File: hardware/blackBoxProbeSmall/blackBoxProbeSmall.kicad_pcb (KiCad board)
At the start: 4 copper layers, 44 x 29 mm, 63 parts, among them J1 USB-ID, J2 JTAG_2X05, J3 JTAG_2X05, J4 DevBoardUartOutput, Q1 Q_NMOS_DUAL, Q2 Q_PMOS_DUAL, U1 MCP1702-MB, U2 USBLC6-2, U3 STM32F103CBT, U4 74X2T45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

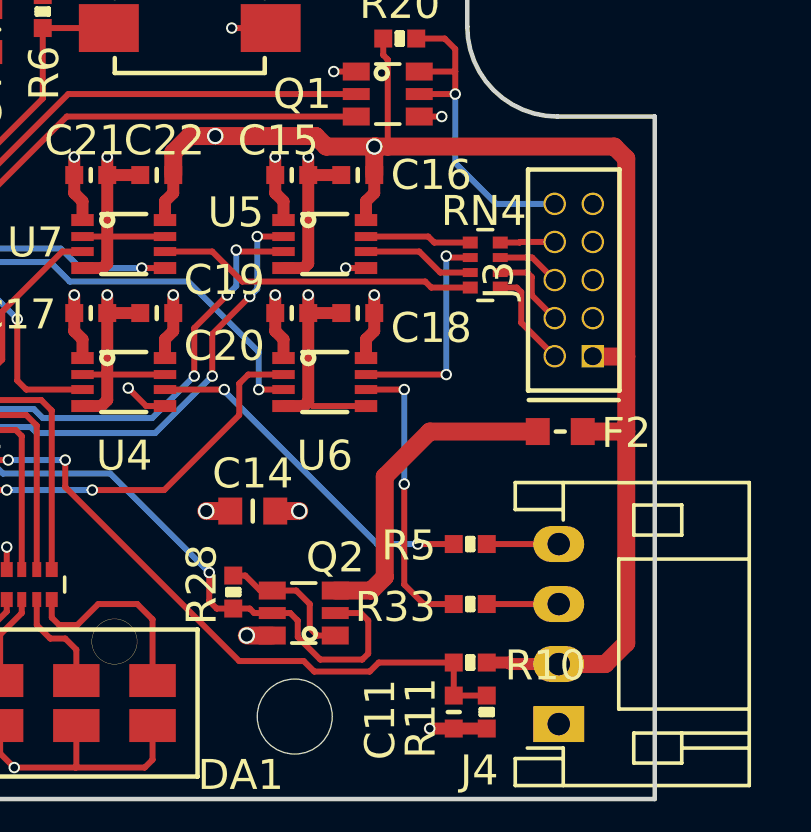
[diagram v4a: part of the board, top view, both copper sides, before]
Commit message: some placement fixes, silk fixes and changed paste aperatures
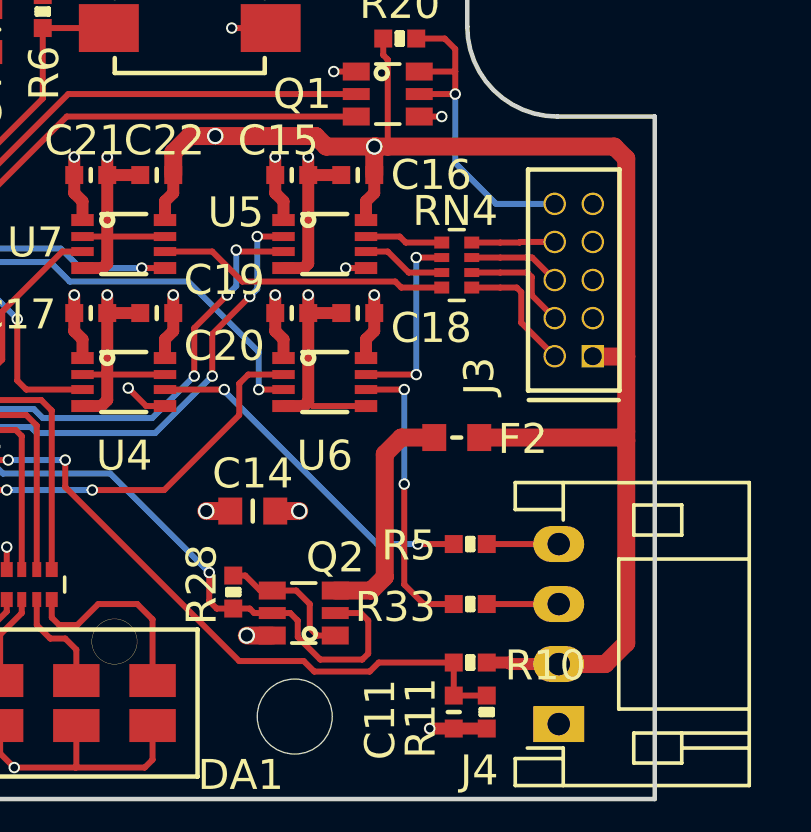
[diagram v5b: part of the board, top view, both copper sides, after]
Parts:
- moved F2 3.46 mm to (161.1, 101.8)
- moved RN4 0.95 mm to (161.1, 96.1)
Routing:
- net /PROBE_VDD: track 64.0 -> 67.4 mm
- net Net-(F2-Pad2): track 10.9 -> 7.81 mm
- net /PROBE_E_TDO: track 7.45 -> 6.43 mm
- net /PROBE_E_TDI: track 3.56 -> 2.61 mm
- net Net-(J3-Pad2): track 3.36 -> 4.31 mm
- net Net-(J3-Pad8): track 1.82 -> 2.77 mm
- net Net-(J3-Pad6): track 2.13 -> 3.08 mm
- net Net-(J3-Pad4): track 2.80 -> 3.75 mm
- net /PROBE_E_TMS: track 10.7 -> 9.72 mm
- net /PROBE_E_TCK: track 3.76 -> 2.81 mm
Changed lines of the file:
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@@
     (thickness 1.6)
     (drawings 10)
-    (tracks 696)
+    (tracks 700)
     (zones 0)
     (modules 63)
@@
   )
   (setup
-    (last_trace_width 0.2)
+    (last_trace_width 0.6)
     (user_trace_width 0.1524)
     (user_trace_width 0.2)
@@
     (pad_to_mask_clearance 0.1)
     (solder_mask_min_width 0.25)
+    (pad_to_paste_clearance_ratio -0.1)
     (aux_axis_origin 0 0)
     (visible_elements FFFFFF7F)
@@
     (add_net "Net-(J2-Pad4)")
     (add_net "Net-(J2-Pad6)")
-    (add_net "Net-(J2-Pad7)")
     (add_net "Net-(J2-Pad8)")
     (add_net "Net-(J3-Pad2)")
     (add_net "Net-(J3-Pad4)")
     (add_net "Net-(J3-Pad6)")
-    (add_net "Net-(J3-Pad7)")
     (add_net "Net-(J3-Pad8)")
     (add_net "Net-(J4-Pad3)")
@@
     (add_net "Net-(R16-Pad2)")
     (add_net "Net-(R27-Pad2)")
-    (add_net "Net-(U3-Pad10)")
-    (add_net "Net-(U3-Pad2)")
-    (add_net "Net-(U3-Pad27)")
-    (add_net "Net-(U3-Pad28)")
-    (add_net "Net-(U3-Pad3)")
-    (add_net "Net-(U3-Pad4)")
-    (add_net "Net-(U3-Pad43)")
-    (add_net "Net-(U3-Pad45)")
-    (add_net "Net-(U3-Pad46)")
   )
   (module SquantorLabels:Label_Generic (layer B.Cu)
@@
   )
   (module Resistor_SMD:R_Array_Convex_4x0402 (layer F.Cu)
-    (at 162.05 96.1)
+    (at 161.1 96.1)
     (descr "Chip Resistor Network, ROHM MNR04 (see mnr_g.pdf)")
     (tags "resistor array")
@@
     (descr "Header 1.27 2by5 pins")
     (tags "Header 1.27")
-    (fp_text reference J3 (at 0 -2.5 90) (layer F.SilkS)
+    (fp_text reference J3 (at -3.2 -3.15 90) (layer F.SilkS)
       (effects (font (size 1 1) (thickness 0.15)))
     )
@@
   )
   (module SquantorRcl:F_0603_hand (layer F.Cu)
-    (at 164.55 101.65 180)
+    (at 161.1 101.85 180)
     (descr "Fuse SMD 0603, reflow soldering")
     (tags "fuse 0603")
@@
   (segment (start 166.05 109.4) (end 166.75 108.7) (width 0.6) (layer F.Cu) (net 5))
   (segment (start 166.75 92.55) (end 166.35 92.15) (width 0.6) (layer F.Cu) (net 5))
-  (segment (start 166.75 101.65) (end 165.3 101.65) (width 0.6) (layer F.Cu) (net 5))
-  (segment (start 166.75 108.7) (end 166.75 101.65) (width 0.6) (layer F.Cu) (net 5))
   (segment (start 166.75 99.15) (end 165.645 99.15) (width 0.6) (layer F.Cu) (net 5))
   (segment (start 165.645 99.15) (end 165.635 99.14) (width 0.6) (layer F.Cu) (net 5))
@@
   (via (at 158.35 92.15) (size 0.55) (drill 0.4) (layers F.Cu B.Cu) (net 5))
   (segment (start 158.35 92.15) (end 158.35 93.1) (width 0.6) (layer F.Cu) (net 5))
+  (segment (start 166.65 101.85) (end 161.85 101.85) (width 0.6) (layer F.Cu) (net 5))
+  (segment (start 166.75 101.95) (end 166.65 101.85) (width 0.6) (layer F.Cu) (net 5))
+  (segment (start 166.75 101.95) (end 166.75 101.65) (width 0.6) (layer F.Cu) (net 5))
+  (segment (start 166.75 108.7) (end 166.75 101.95) (width 0.6) (layer F.Cu) (net 5))
   (segment (start 164.365 99.14) (end 163.25 98.025) (width 0.2) (layer F.Cu) (net 6))
   (segment (start 163.25 98.025) (end 163.25 97) (width 0.2) (layer F.Cu) (net 6))
   (segment (start 163.1 96.85) (end 162.55 96.85) (width 0.2) (layer F.Cu) (net 6))
   (segment (start 163.25 97) (end 163.1 96.85) (width 0.2) (layer F.Cu) (net 6))
+  (segment (start 162.55 96.85) (end 161.6 96.85) (width 0.2) (layer F.Cu) (net 6))
   (segment (start 164.365 96.6) (end 163.615 95.85) (width 0.2) (layer F.Cu) (net 7))
   (segment (start 163.615 95.85) (end 162.55 95.85) (width 0.2) (layer F.Cu) (net 7))
+  (segment (start 162.55 95.85) (end 161.6 95.85) (width 0.2) (layer F.Cu) (net 7))
   (segment (start 164.5 107.4) (end 162.1 107.4) (width 0.2) (layer F.Cu) (net 8))
   (segment (start 148.15 90.4) (end 157.75 90.4) (width 0.2) (layer F.Cu) (net 9))
@@
   (segment (start 134.7 95.85) (end 135.2 95.35) (width 0.2) (layer F.Cu) (net 21))
   (segment (start 132.75 98.55) (end 132.25 98.05) (width 0.2) (layer F.Cu) (net 21))
-  (segment (start 161.55 96.35) (end 160.55 96.35) (width 0.2) (layer F.Cu) (net 23))
-  (segment (start 159.85 95.65) (end 158.075 95.65) (width 0.2) (layer F.Cu) (net 23))
-  (segment (start 160.55 96.35) (end 159.85 95.65) (width 0.2) (layer F.Cu) (net 23))
-  (segment (start 161.55 95.35) (end 160.35 95.35) (width 0.2) (layer F.Cu) (net 24))
-  (segment (start 160.15 95.15) (end 158.075 95.15) (width 0.2) (layer F.Cu) (net 24))
-  (segment (start 160.35 95.35) (end 160.15 95.15) (width 0.2) (layer F.Cu) (net 24))
-  (segment (start 161.55 96.85) (end 160.25 96.85) (width 0.2) (layer F.Cu) (net 25))
-  (segment (start 160.25 96.85) (end 160.05 96.65) (width 0.2) (layer F.Cu) (net 25))
-  (segment (start 160.05 96.65) (end 153.95 96.65) (width 0.2) (layer F.Cu) (net 25))
+  (segment (start 158.8 95.65) (end 158.075 95.65) (width 0.2) (layer F.Cu) (net 23))
+  (segment (start 159.5 96.35) (end 158.8 95.65) (width 0.2) (layer F.Cu) (net 23))
+  (segment (start 160.6 96.35) (end 159.5 96.35) (width 0.2) (layer F.Cu) (net 23))
+  (segment (start 159.2 95.15) (end 158.075 95.15) (width 0.2) (layer F.Cu) (net 24))
+  (segment (start 159.4 95.35) (end 159.2 95.15) (width 0.2) (layer F.Cu) (net 24))
+  (segment (start 160.6 95.35) (end 159.4 95.35) (width 0.2) (layer F.Cu) (net 24))
   (segment (start 152.95 95.65) (end 151.375 95.65) (width 0.2) (layer F.Cu) (net 25))
   (segment (start 153.95 96.65) (end 152.95 95.65) (width 0.2) (layer F.Cu) (net 25))
-  (via (at 160.75 95.8) (size 0.381) (drill 0.254) (layers F.Cu B.Cu) (net 26))
-  (segment (start 161.55 95.85) (end 160.8 95.85) (width 0.2) (layer F.Cu) (net 26))
-  (segment (start 160.8 95.85) (end 160.75 95.8) (width 0.2) (layer F.Cu) (net 26))
-  (segment (start 160.75 95.8) (end 160.75 99.65) (width 0.2) (layer B.Cu) (net 26))
-  (via (at 160.75 99.75) (size 0.381) (drill 0.254) (layers F.Cu B.Cu) (net 26))
-  (segment (start 160.75 99.65) (end 160.75 99.75) (width 0.2) (layer B.Cu) (net 26))
-  (segment (start 160.75 99.75) (end 158.075 99.75) (width 0.2) (layer F.Cu) (net 26))
+  (segment (start 159.05 96.65) (end 153.95 96.65) (width 0.2) (layer F.Cu) (net 25))
+  (segment (start 159.25 96.85) (end 159.05 96.65) (width 0.2) (layer F.Cu) (net 25))
+  (segment (start 160.6 96.85) (end 159.25 96.85) (width 0.2) (layer F.Cu) (net 25))
+  (segment (start 159.75 99.75) (end 158.075 99.75) (width 0.2) (layer F.Cu) (net 26))
+  (via (at 159.75 99.75) (size 0.381) (drill 0.254) (layers F.Cu B.Cu) (net 26))
+  (segment (start 159.75 95.85) (end 159.75 99.75) (width 0.2) (layer B.Cu) (net 26))
+  (via (at 159.75 95.85) (size 0.381) (drill 0.254) (layers F.Cu B.Cu) (net 26))
+  (segment (start 160.6 95.85) (end 159.75 95.85) (width 0.2) (layer F.Cu) (net 26))
   (segment (start 146.6 101.8) (end 146.6 106.25) (width 0.2) (layer F.Cu) (net 27))
   (segment (start 141.875 101.6) (end 146.4 101.6) (width 0.2) (layer F.Cu) (net 27))
@@
   (via (at 152.75 104.3) (size 0.55) (drill 0.4) (layers F.Cu B.Cu) (net 50))
   (segment (start 153.55 104.3) (end 152.75 104.3) (width 0.6) (layer F.Cu) (net 50))
-  (segment (start 163.8 101.65) (end 160.2 101.65) (width 0.6) (layer F.Cu) (net 55))
-  (segment (start 160.2 101.65) (end 158.7 103.15) (width 0.6) (layer F.Cu) (net 55))
-  (segment (start 158.7 103.15) (end 158.7 106.5) (width 0.6) (layer F.Cu) (net 55))
-  (segment (start 158.25 106.95) (end 157.05 106.95) (width 0.6) (layer F.Cu) (net 55))
-  (segment (start 158.7 106.5) (end 158.25 106.95) (width 0.6) (layer F.Cu) (net 55))
+  (segment (start 158.7 102.4) (end 159.25 101.85) (width 0.6) (layer F.Cu) (net 55))
+  (segment (start 158.7 106.5) (end 158.7 102.4) (width 0.6) (layer F.Cu) (net 55))
+  (segment (start 157.05 106.95) (end 158.25 106.95) (width 0.6) (layer F.Cu) (net 55))
+  (segment (start 159.25 101.85) (end 160.35 101.85) (width 0.6) (layer F.Cu) (net 55))
+  (segment (start 158.25 106.95) (end 158.7 106.5) (width 0.6) (layer F.Cu) (net 55))
   (segment (start 130.55 103.83) (end 130.55 102.5) (width 0.2) (layer F.Cu) (net 56))
   (segment (start 127.035 104.02) (end 130.36 104.02) (width 0.2) (layer F.Cu) (net 56))
@@
   (segment (start 163.2 95.35) (end 162.55 95.35) (width 0.2) (layer F.Cu) (net 60))
   (segment (start 163.22 95.33) (end 163.2 95.35) (width 0.2) (layer F.Cu) (net 60))
+  (segment (start 162.55 95.35) (end 161.6 95.35) (width 0.2) (layer F.Cu) (net 60))
   (segment (start 164.365 97.87) (end 163.6 97.105) (width 0.2) (layer F.Cu) (net 61))
   (segment (start 163.6 97.105) (end 163.6 96.5) (width 0.2) (layer F.Cu) (net 61))
   (segment (start 163.45 96.35) (end 162.55 96.35) (width 0.2) (layer F.Cu) (net 61))
   (segment (start 163.6 96.5) (end 163.45 96.35) (width 0.2) (layer F.Cu) (net 61))
+  (segment (start 162.55 96.35) (end 161.6 96.35) (width 0.2) (layer F.Cu) (net 61))
   (segment (start 164.5 105.4) (end 162.1 105.4) (width 0.2) (layer F.Cu) (net 62))
   (zone (net 48) (net_name /VSS) (layer In1.Cu) (hatch edge 0.508)

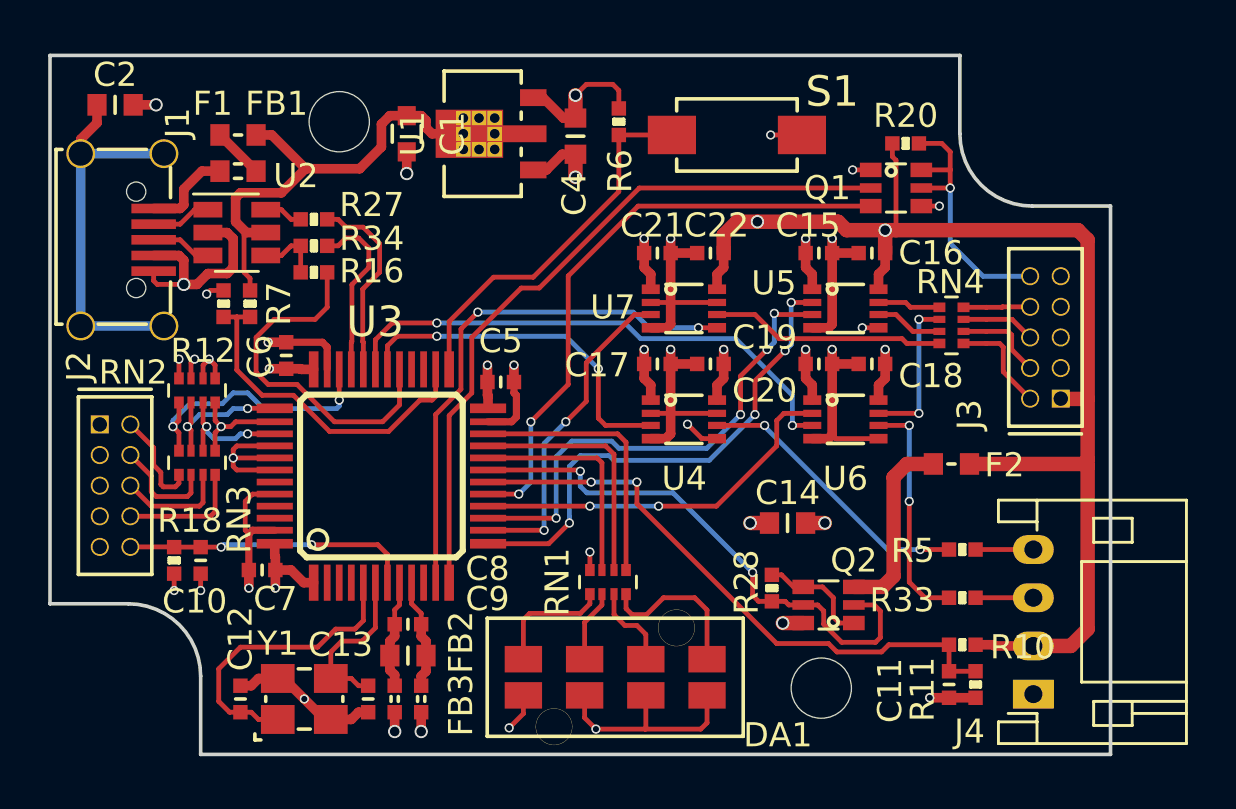
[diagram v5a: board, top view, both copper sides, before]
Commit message: silk placement mistakes fixed, removed groundplane under crystal
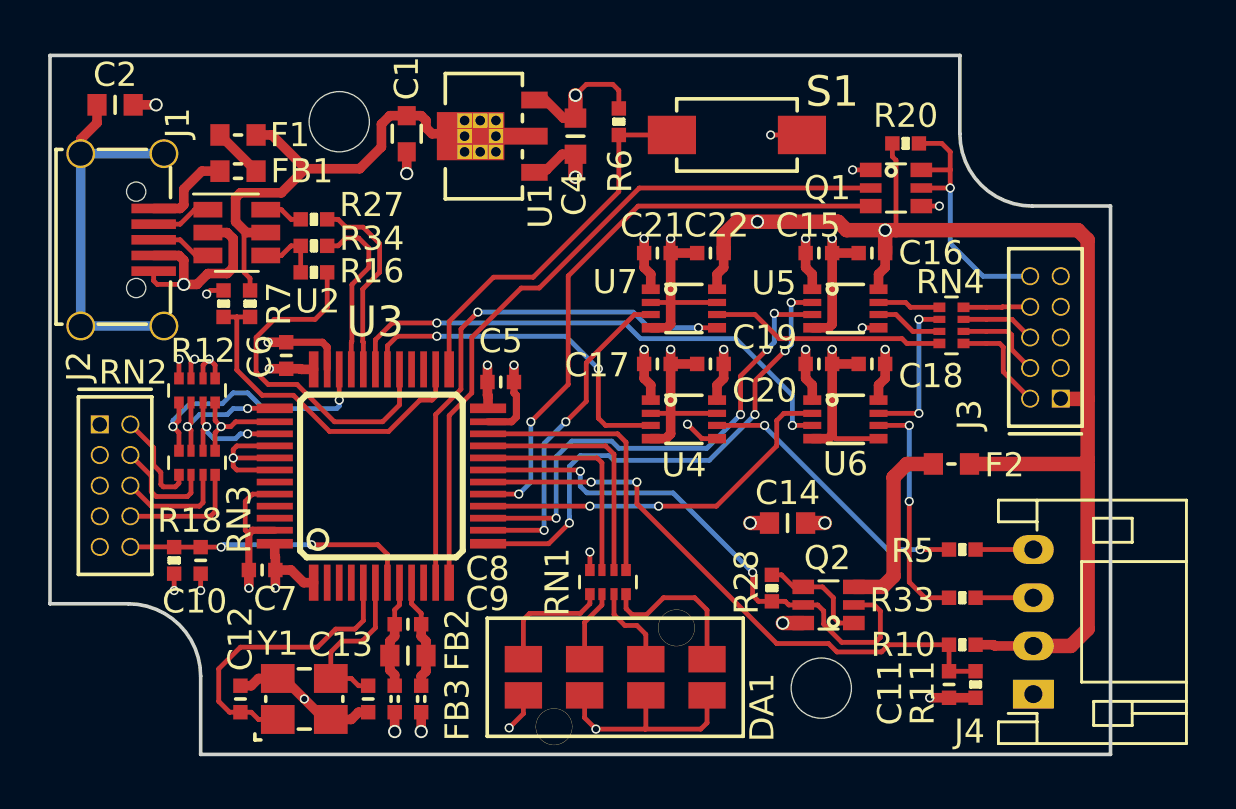
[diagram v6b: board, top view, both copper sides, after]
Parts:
- moved U1 0.11 mm to (142.1, 88.2)
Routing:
- net /VSS: track 81.6 -> 87.3 mm

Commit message: further beautification and some trace reroutings
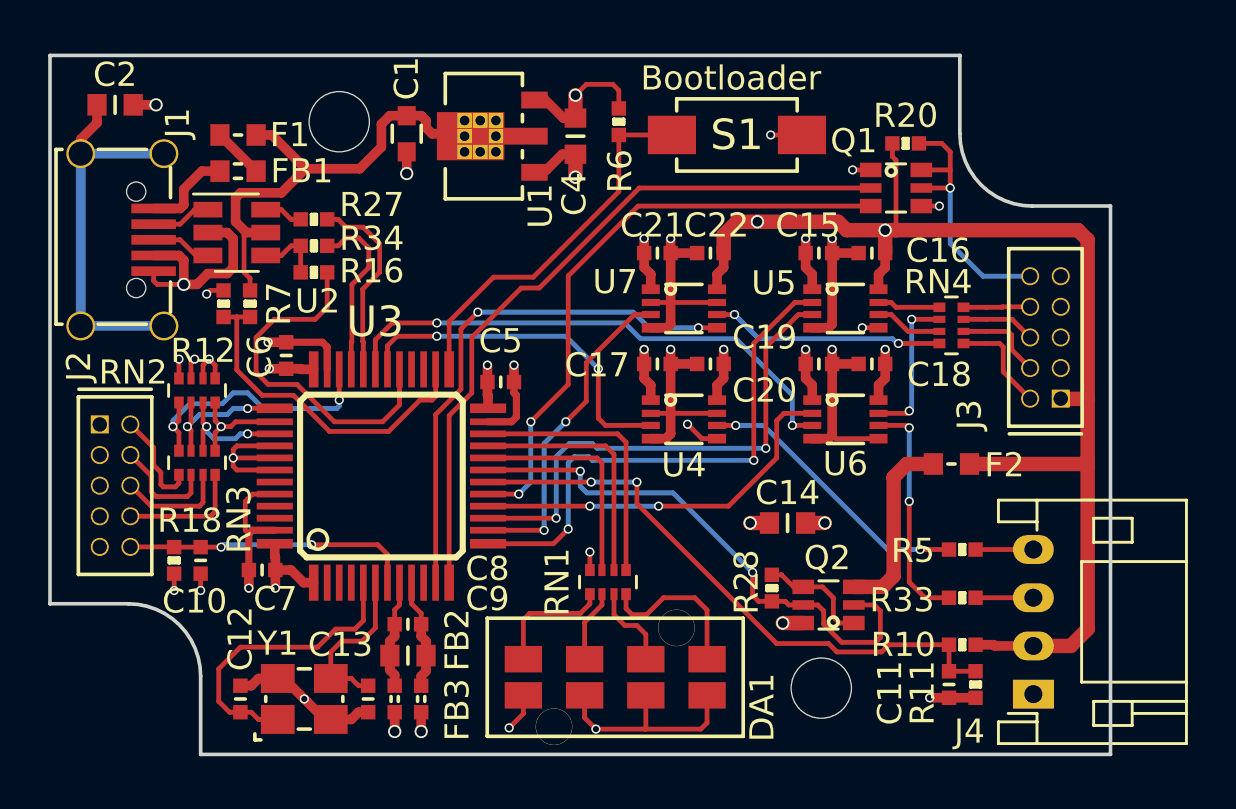
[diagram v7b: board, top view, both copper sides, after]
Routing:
- net /PROBE_I_TDI: track 21.0 -> 22.2 mm, vias 4 -> 2
- net /PROBE_I_TCK: track 20.4 -> 21.1 mm, vias 4 -> 2
- net /PROBE_E_TMS: vias 0 -> 2
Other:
- board text added: "Bootloader"
